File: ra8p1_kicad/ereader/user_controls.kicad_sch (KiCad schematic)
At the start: 20 parts, among them SW2 PAGE_PREV, SW3 PAGE_NEXT, SW4 VOL_DOWN, SW5 VOL_UP

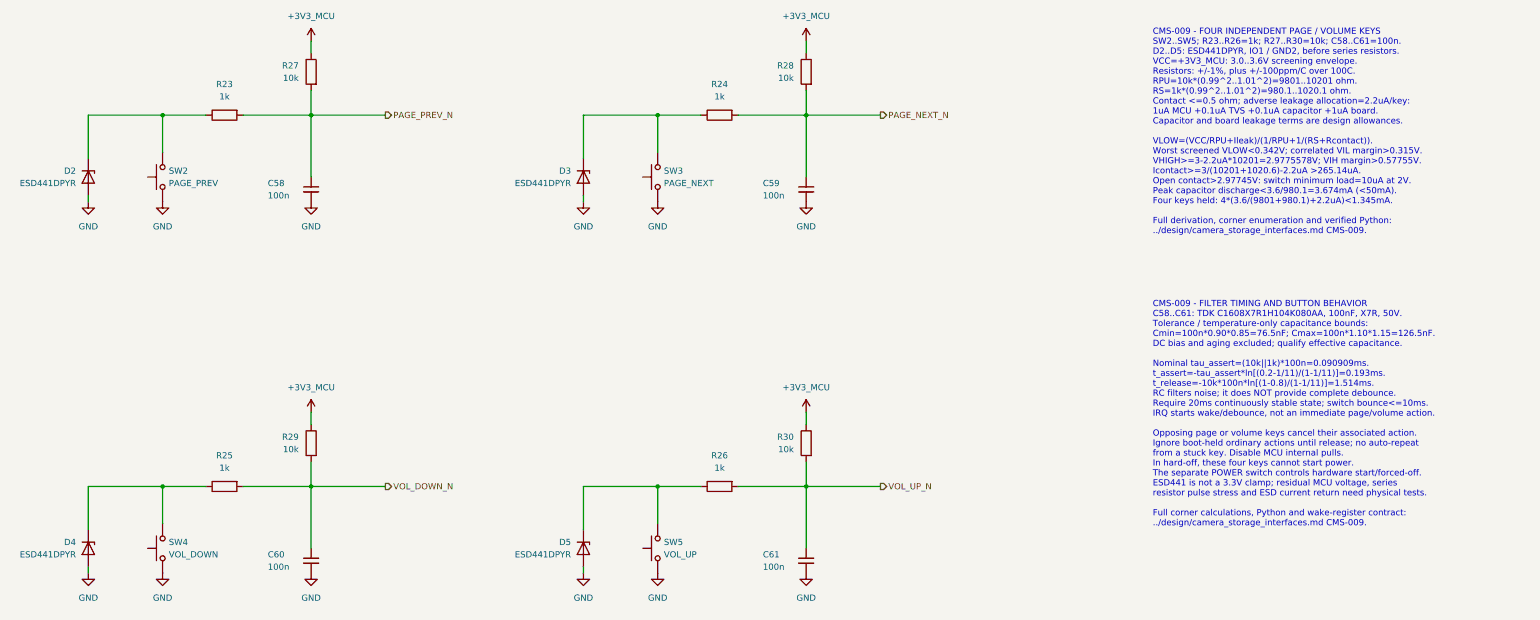
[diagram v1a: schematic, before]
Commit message: wip(hardware): preserve schematic cleanup and CEU host ports
Checkpoint cosmetic cleanup across the schematic hierarchy and eleven parallel-camera host ports. Refresh the complete 13-page PDF. All 334 existing net partitions and 271 component records match the prior CEU checkpoint; all 128 ERC identities remain unchanged. Electrical design is incomplete; this is a WIP checkpoint for #821 and #841.
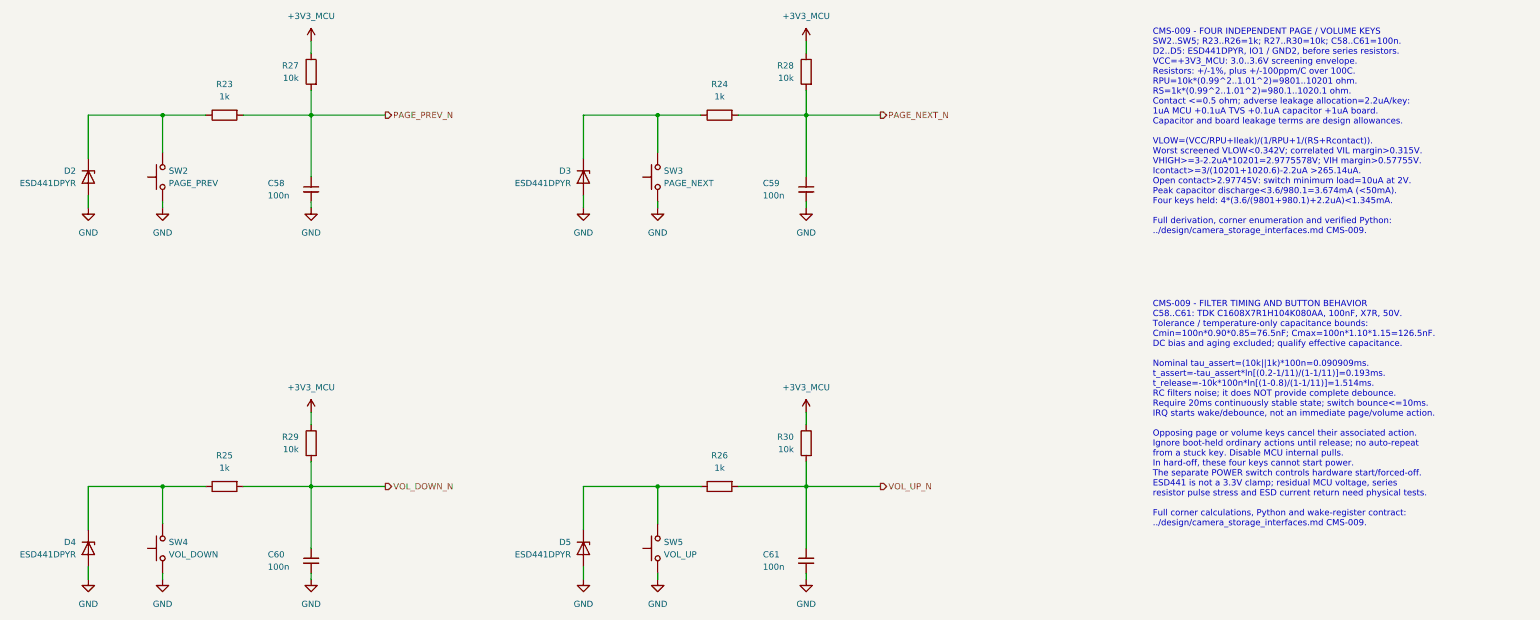
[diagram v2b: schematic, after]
